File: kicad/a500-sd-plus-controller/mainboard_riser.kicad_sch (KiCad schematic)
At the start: 4 parts, among them J1 DIP_socket_48pins, U1 CSG5719_Gary, U4 CSG8520_CIA, U5 DIP_socket_40pins

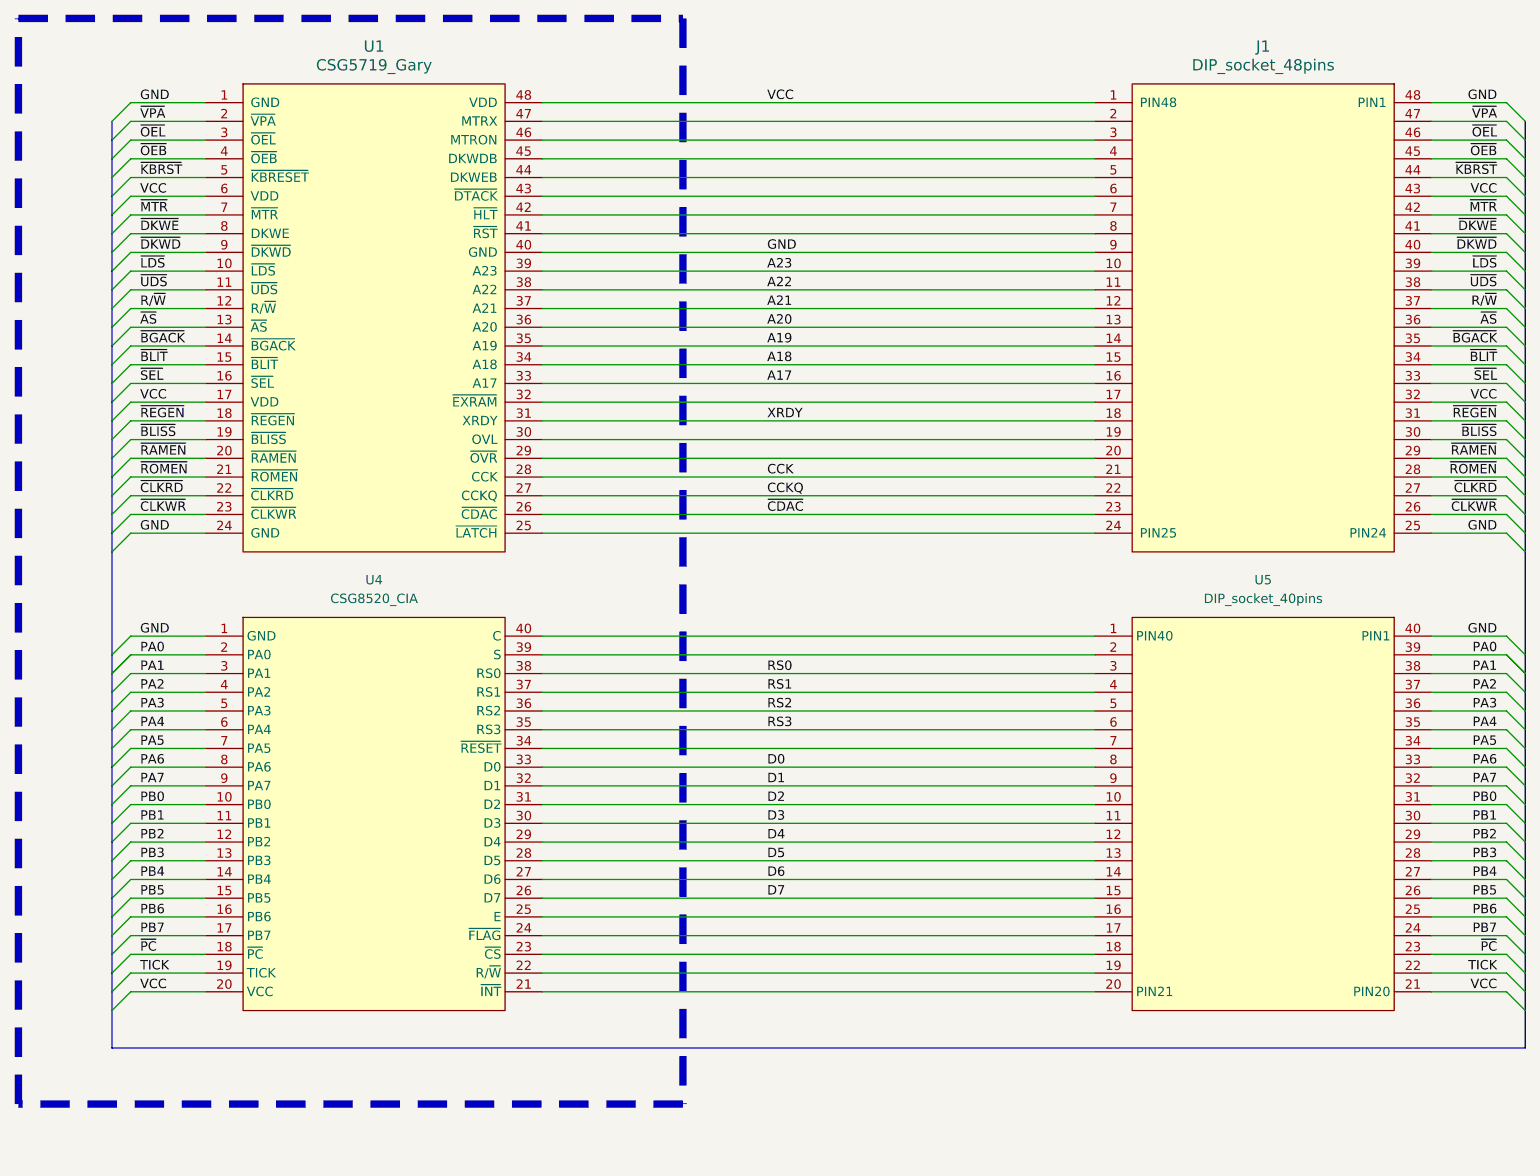
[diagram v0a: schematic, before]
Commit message: more work done on hardware
basic schematic done
layout in progress
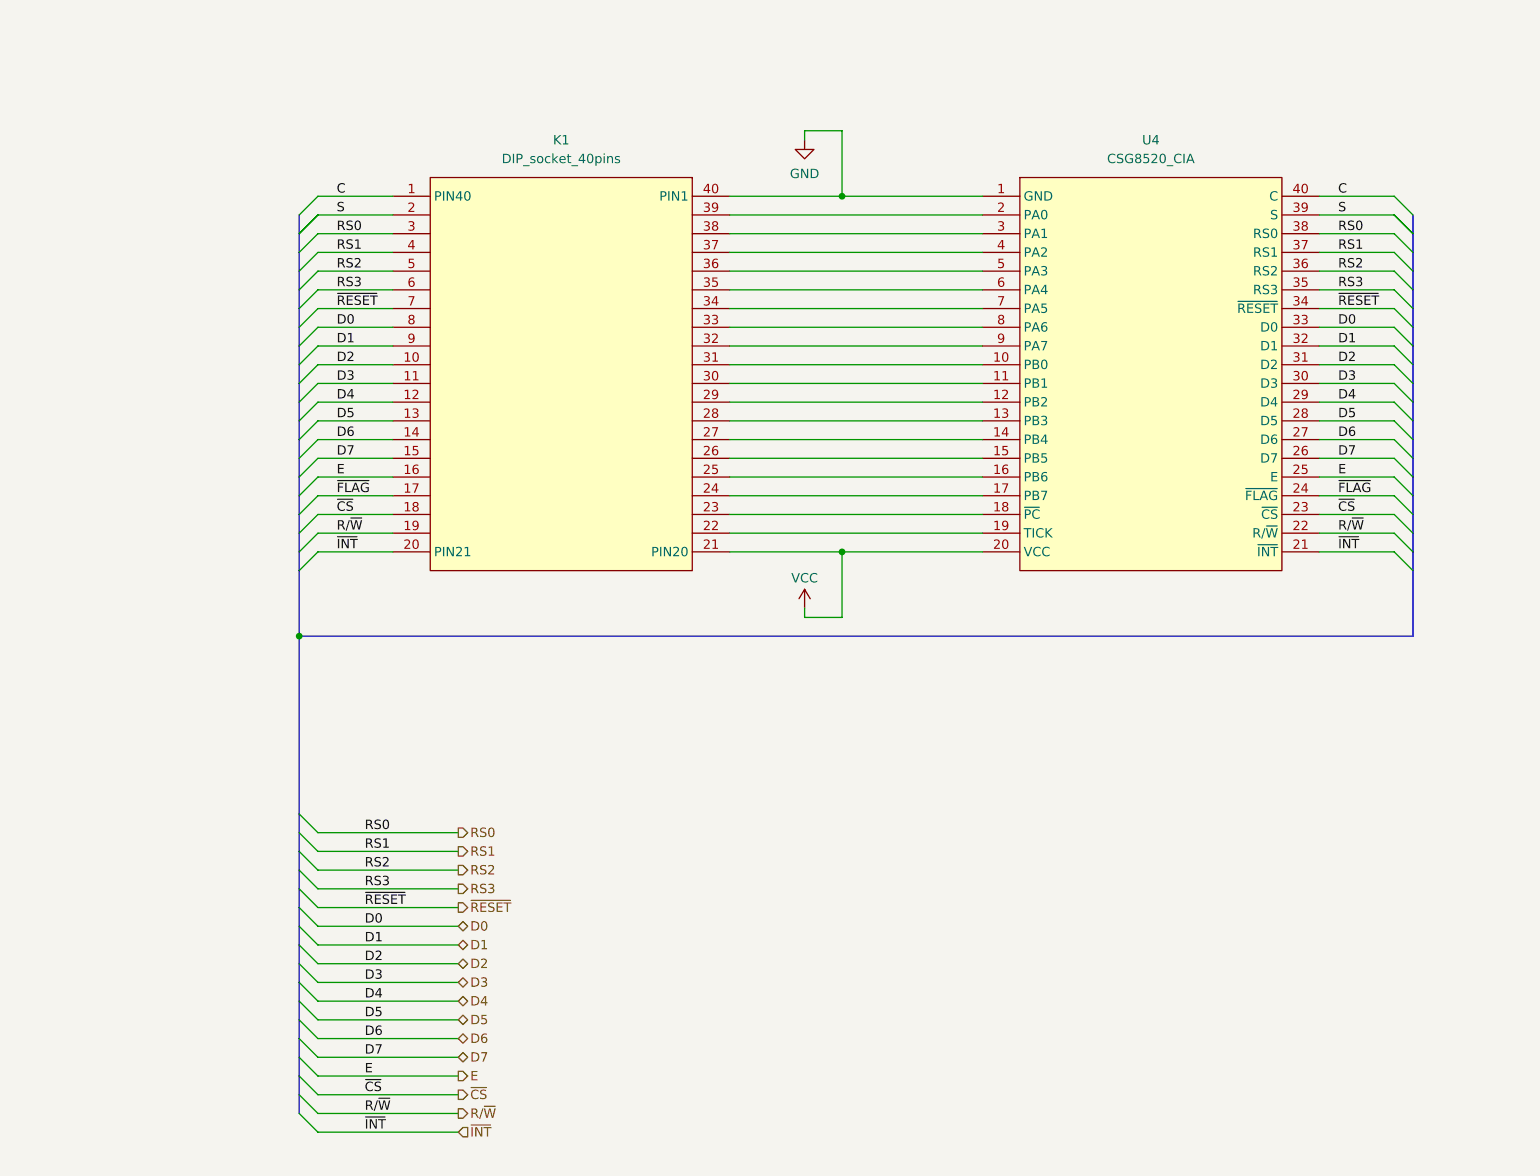
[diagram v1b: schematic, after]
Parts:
- removed J1: DIP_socket_48pins, Package_DIP:DIP-48_W15.24mm_Socket, symbol Dennis:DIP_socket_48pins
- removed U1: CSG5719_Gary, Package_DIP:DIP-48_W15.24mm_Socket, symbol Dennis:CSG5719_Gary
- K1: renamed from U5; footprint (none) -> Package_DIP:DIP-40_W15.24mm
- U4: footprint (none) -> Package_DIP:DIP-40_W15.24mm
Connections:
- net R/~{W}: now also K1.19, U4.22 (R/~{W})
- net ~{INT}: now reaches K1.20 (PIN21), U4.21 (~{INT})
- net ~{CS}: now reaches K1.18, U4.23 (~{CS})
- net ~{FLAG}: now reaches K1.17, U4.24 (~{FLAG})
- net E: now reaches K1.16, U4.25 (E)
- net ~{RESET}: now reaches K1.7, U4.34 (~{RESET})
- net S: now reaches K1.2, U4.39 (S)
- net C: now reaches K1.1 (PIN40), U4.40 (C)
- net PA0: no longer names the net of K1.39, U4.2 (PA0)
- net PA1: no longer names the net of K1.38, U4.3 (PA1)
- net PA2: no longer names the net of K1.37, U4.4 (PA2)
- net PA3: no longer names the net of K1.36, U4.5 (PA3)
- net PA4: no longer names the net of K1.35, U4.6 (PA4)
- net PA5: no longer names the net of K1.34, U4.7 (PA5)
- net PA6: no longer names the net of K1.33, U4.8 (PA6)
- net PA7: no longer names the net of K1.32, U4.9 (PA7)
- net PB0: no longer names the net of K1.31, U4.10 (PB0)
- net PB1: no longer names the net of K1.30, U4.11 (PB1)
- net PB2: no longer names the net of K1.29, U4.12 (PB2)
- net PB3: no longer names the net of K1.28, U4.13 (PB3)
- net PB4: no longer names the net of K1.27, U4.14 (PB4)
- net PB5: no longer names the net of K1.26, U4.15 (PB5)
- net PB6: no longer names the net of K1.25, U4.16 (PB6)
- net PB7: no longer names the net of K1.24, U4.17 (PB7)
- net TICK: no longer names the net of K1.22, U4.19 (TICK)
- net ~{PC}: no longer names the net of K1.23, U4.18 (~{PC})
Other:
- moved on the sheet: K1, U4

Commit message: added add ethernet controller
still work in progress
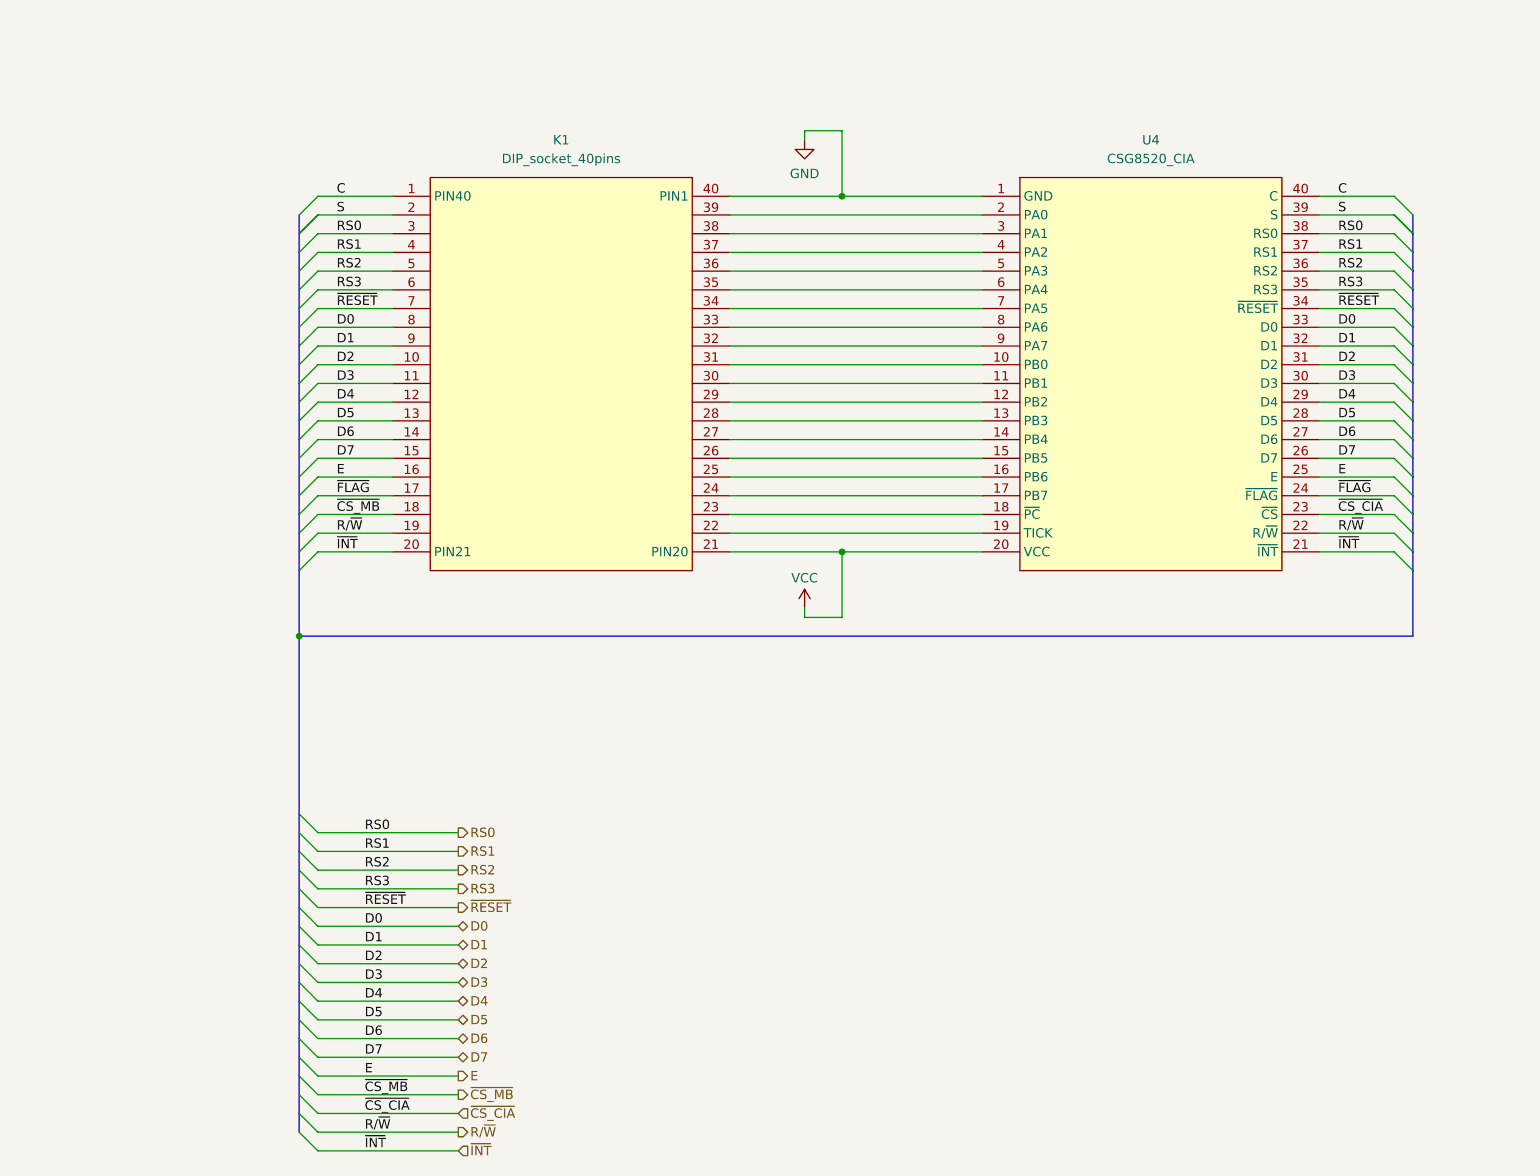
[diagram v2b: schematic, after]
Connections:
- net ~{CS} renamed ~{CS_CIA}
- net ~{CS_CIA}: no longer K1.18
- new net ~{CS_MB}: K1.18
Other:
- company: Mathesar -> Dennis van Weeren
- title: A500-SD-plus-controller -> A500 SD plus controller

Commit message: PCB done, this version has been sent to fabrication
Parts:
- K1, U4: Quantity (none) -> ${QUANTITY}
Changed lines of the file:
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@@
+			)
+		)
+		(property "Quantity" "${QUANTITY}"
+			(at 189.23 64.77 0)
+			(effects
+				(font
+					(size 1.27 1.27)
+				)
+				(hide yes)
 			)
 		)
@@
 			(at 109.22 64.77 0)
 			(effects
+				(font
+					(size 1.27 1.27)
+				)
+				(hide yes)
+			)
+		)
+		(property "Quantity" "${QUANTITY}"
+			(at 109.22 64.77 0)
+			(effects
